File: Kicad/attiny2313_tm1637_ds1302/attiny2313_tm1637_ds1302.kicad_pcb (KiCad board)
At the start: 2 copper layers, 15 parts, among them Q1 S9014, U1 ATtiny2313A-PU, U2 DS1302+, U3 tm1637-module, Y1 Crystal

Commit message: created PCB
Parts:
- removed BT1: Battery_Cell, Battery:BatteryHolder_Keystone_103_1x20mm
- added J1: Conn_01x02, Battery:power_pins_smd, F.Cu at (108.5, 97.5)
- added J2: Conn_01x04, Connector:conn_01x04, F.Cu at (161.5, 94.5)
- added J3: Conn_01x04, Connector:conn_01x04, F.Cu at (177.3, 87.9)
- D1, D2: footprint Diode_THT:D_DO-15_P12.70mm_Horizontal -> Diode_THT:D_DO-15_P3.81mm_Vertical_KathodeUp
- Q1: footprint Package_TO_SOT_THT:TO-39-3 -> Package_TO_SOT_THT:SIPAK_Vertical
- R1, R2: footprint Resistor_THT:R_Axial_DIN0309_L9.0mm_D3.2mm_P12.70mm_Horizontal -> Resistor_THT:R_Axial_DIN0309_L9.0mm_D3.2mm_P5.08mm_Vertical
- U3: moved to B.Cu
- moved BZ1 841.8 mm to (146.3, 90.9)
- moved U1 824.3 mm to (145.0, 74.4), turned to 270 degrees
- moved SW_3 816.4 mm to (184.2, 96.3), turned to 270 degrees
- moved SW_2 813.2 mm to (184.2, 84.8), turned to 270 degrees
- moved U3 801.3 mm to (141.2, 85.9), turned to 180 degrees
- moved SW_1 799.9 mm to (184.2, 73.4), turned to 270 degrees
- moved R1 773.5 mm to (113.3, 77.0), turned to 180 degrees
- moved D1 769.2 mm to (166.6, 75.7), turned to 180 degrees
- moved D2 761.6 mm to (161.0, 83.3), turned to 270 degrees
- moved R2 757.3 mm to (155.2, 75.7), turned to 180 degrees
- moved U2 754.9 mm to (119.6, 87.1)
- moved Q1 748.5 mm to (150.4, 82.0)
- moved R3 727.5 mm to (137.4, 90.9), turned to 90 degrees
- moved Y1 727.4 mm to (117.1, 90.9), turned to 180 degrees
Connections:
- net CLK renamed Net-(U1-Pad12)
- net DIO renamed Net-(U1-Pad13)
- R1 pad 1: Net-(R1-Pad1) -> Net-(BZ1-Pad1)
- SW_1 pad 1: Net-(D1-Pad1) -> Net-(J3-Pad1)
- SW_1 pad 2: GND -> Net-(J3-Pad4)
- SW_2 pad 1: Net-(D2-Pad1) -> Net-(J3-Pad3)
- SW_2 pad 2: GND -> Net-(J3-Pad4)
- SW_3 pad 1: Net-(D1-Pad2) -> Net-(J3-Pad2)
- SW_3 pad 2: GND -> Net-(J3-Pad4)
- U1 pad 11: Net-(U1-Pad11) -> (no net)
- U1 pad 18: Net-(U1-Pad18) -> (no net)
- U1 pad 19: Net-(U1-Pad19) -> (no net)
- U1 pad 2: Net-(U1-Pad2) -> (no net)
- U1 pad 20: Net-(R1-Pad1) -> Net-(BZ1-Pad1)
- U1 pad 3: Net-(U1-Pad3) -> (no net)
- U1 pad 4: Net-(U1-Pad4) -> (no net)
- U1 pad 5: Net-(U1-Pad5) -> (no net)
- U1 pad 8: Net-(U1-Pad8) -> (no net)
- U1 pad 9: Net-(U1-Pad9) -> (no net)
- U2 pad 1: Net-(U2-Pad1) -> (no net)
- U2 pad 8: Net-(BT1-Pad1) -> (no net)
- U3 pad 1: Net-(U3-Pad1) -> Net-(BZ1-Pad1)
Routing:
- net Net-(BZ1-Pad1): track 0.00 -> 88.2 mm
- net Net-(U1-Pad13): track 0.00 -> 84.7 mm
- net Net-(U1-Pad12): track 0.00 -> 75.2 mm
- net Net-(D1-Pad1): track 0.00 -> 70.1 mm
- net Net-(D2-Pad1): track 0.00 -> 49.9 mm
- net Net-(R1-Pad2): track 0.00 -> 39.3 mm
- net Net-(D1-Pad2): track 0.00 -> 34.4 mm
- net Net-(J3-Pad2): track 0.00 -> 23.3 mm
- net Net-(R2-Pad2): track 0.00 -> 23.0 mm
- net Net-(J3-Pad1): track 0.00 -> 18.2 mm
- net Net-(Q1-Pad1): track 0.00 -> 18.1 mm
- net Net-(J3-Pad3): track 0.00 -> 16.9 mm
- net RST: track 0.00 -> 16.7 mm
- net I\O: track 0.00 -> 14.4 mm
- net SCLK: track 0.00 -> 10.8 mm
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- added copper zone on F.Cu, net GND
- added copper zone on F.Cu, net Net-(J3-Pad4)
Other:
- board outline added: 84.3 x 35.1 mm
- board text added: "Button panel"
- board text added: "rev 1.0"

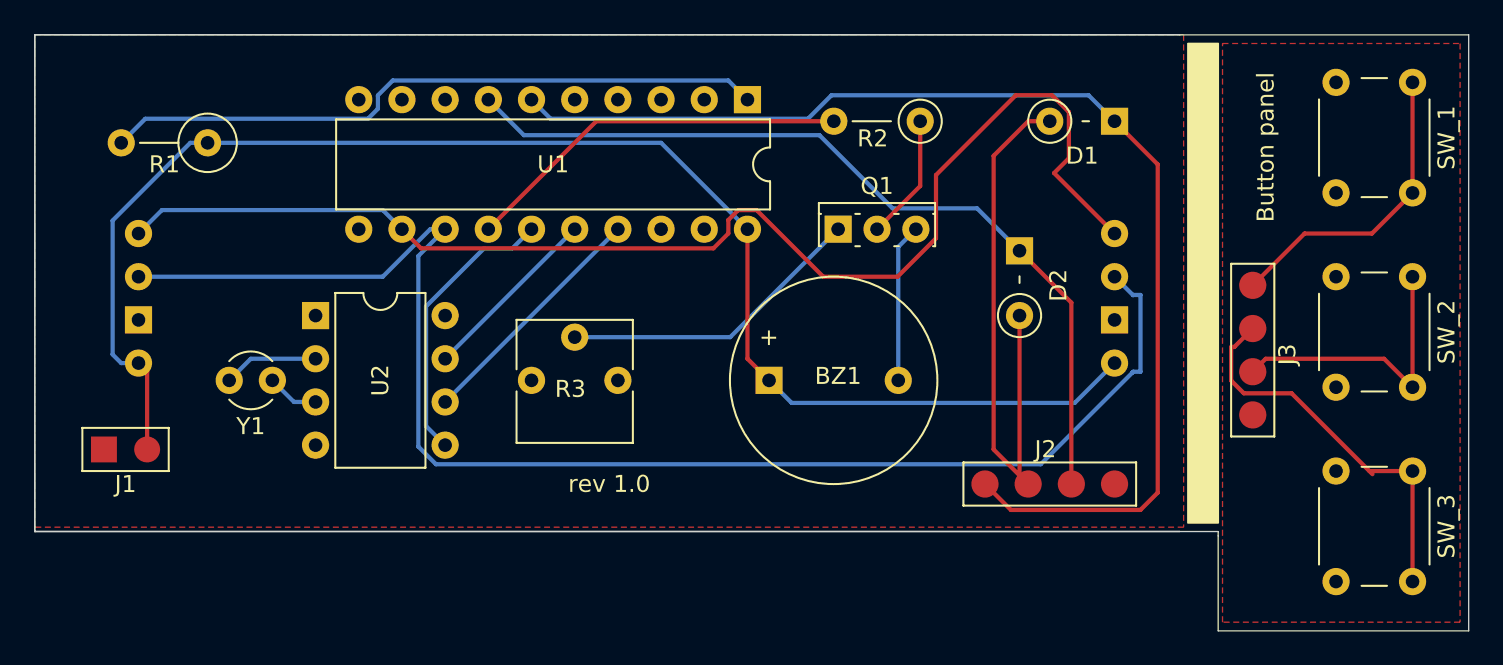
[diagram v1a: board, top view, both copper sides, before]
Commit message: убрана регулировка яркости, убрана кнопка яркости
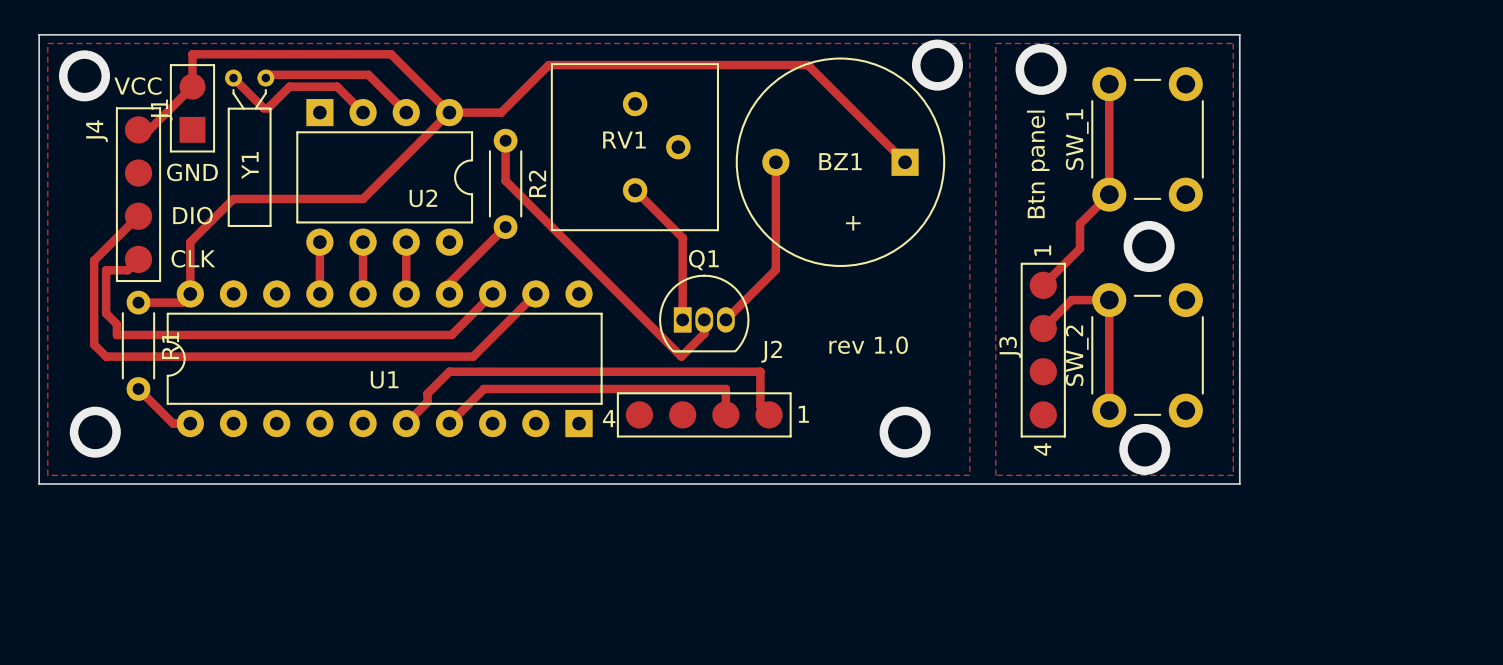
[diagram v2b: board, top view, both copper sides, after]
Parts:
- removed D1, D2: DIODE, Diode_THT:D_DO-15_P3.81mm_Vertical_KathodeUp
- removed R3: R_Variable, Potentiometer_THT:Potentiometer_Vishay_T73YP_Vertical
- removed SW_3: Brightness, Button_Switch_THT:SW_PUSH_6mm
- removed U3: tm1637-module, Module:tm1637-module
- added J4: Conn_01x04, Connector:conn_01x04, F.Cu at (106.7, 81.3)
- added RV1: R_POT, Potentiometer_THT:Potentiometer_Bourns_3386P_Vertical, F.Cu at (138.4, 79.8)
- Q1: footprint Package_TO_SOT_THT:SIPAK_Vertical -> Package_TO_SOT_THT:TO-92_Inline
- R1, R2: footprint Resistor_THT:R_Axial_DIN0309_L9.0mm_D3.2mm_P5.08mm_Vertical -> Resistor_THT:R_Axial_DIN0204_L3.6mm_D1.6mm_P5.08mm_Horizontal
- SW_2: value Clock_mode -> Clock_Set
- Y1: footprint Crystal:Crystal_AT310_D3.0mm_L10.0mm_Vertical -> Crystal:Crystal_C26-LF_D2.1mm_L6.5mm_Horizontal
- moved U1 37.9 mm to (112.3, 93.5), turned to 90 degrees
- moved R2 24.4 mm to (130.8, 76.8), turned to 270 degrees
- moved J1 23.5 mm to (114.9, 74.9), turned to 270 degrees
- moved SW_2 19.5 mm to (166.3, 92.7), turned to 90 degrees
- moved SW_1 19.0 mm to (166.3, 80.0), turned to 90 degrees
- moved Y1 17.9 mm to (114.8, 73.2), turned to 0 degrees
- moved J2 17.8 mm to (143.8, 95.5), turned to 180 degrees
- moved BZ1 15.1 mm to (154.3, 78.1), turned to 180 degrees
- moved U2 14.3 mm to (127.5, 75.2), turned to 270 degrees
- moved J3 12.3 mm to (165.0, 87.9)
- moved Q1 10.6 mm to (141.2, 87.4)
- moved R1 10.2 mm to (109.2, 86.4), turned to 270 degrees
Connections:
- J2 pad 2: Net-(D1-Pad2) -> Net-(J2-Pad2)
- J2 pad 3: Net-(D2-Pad1) -> Net-(J2-Pad3)
- SW_2 pad 1: Net-(J3-Pad3) -> Net-(J3-Pad2)
- U1 pad 11: (no net) -> Net-(U1-Pad11)
- U1 pad 15: RST -> SCLK
- U1 pad 16: SCLK -> I\O
- U1 pad 17: I\O -> RST
- U1 pad 18: (no net) -> Net-(U1-Pad18)
- U1 pad 19: (no net) -> Net-(U1-Pad19)
- U1 pad 2: (no net) -> Net-(U1-Pad2)
- U1 pad 3: (no net) -> Net-(U1-Pad3)
- U1 pad 4: (no net) -> Net-(U1-Pad4)
- U1 pad 5: (no net) -> Net-(U1-Pad5)
- U1 pad 7: Net-(D2-Pad1) -> Net-(J2-Pad2)
- U1 pad 8: (no net) -> Net-(U1-Pad8)
- U1 pad 9: (no net) -> Net-(U1-Pad9)
- U2 pad 1: (no net) -> Net-(BZ1-Pad1)
- U2 pad 8: (no net) -> Net-(U2-Pad8)
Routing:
- net Net-(J4-Pad1): track 84.7 -> 29.3 mm
- net Net-(D2-Pad1): track 49.9 -> 0.00 mm
- net Net-(J2-Pad1): track 70.1 -> 25.1 mm
- net Net-(J4-Pad2): track 75.2 -> 36.4 mm
- net Net-(R1-Pad2): track 39.3 -> 3.89 mm
- net Net-(D1-Pad2): track 34.4 -> 0.00 mm
- net Net-(J2-Pad2): track 0.00 -> 18.6 mm
- net Net-(R2-Pad2): track 23.0 -> 5.30 mm
- net Net-(J3-Pad3): track 16.9 -> 0.00 mm
- net RST: track 16.7 -> 3.05 mm
- net Net-(Q1-Pad2): track 7.40 -> 19.7 mm
- net Net-(J3-Pad2): track 23.3 -> 11.1 mm
- net I\O: track 14.4 -> 3.05 mm
- net Net-(BZ1-Pad1): track 88.2 -> 77.7 mm
- net Net-(Q1-Pad1): track 18.1 -> 8.78 mm
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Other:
- board size 84.3 x 35.1 mm -> 70.6 x 26.4 mm
- board text added: "1"
- board text added: "4"
- board text added: "Btn panel"
- board text added: "CLK"
- board text added: "DIO"
- board text added: "GND"
- board text added: "VCC"
- board text removed: "Button panel"
